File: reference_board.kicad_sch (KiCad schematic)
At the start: 5 parts, among them J1 CONN_02X04, U1 TMP236

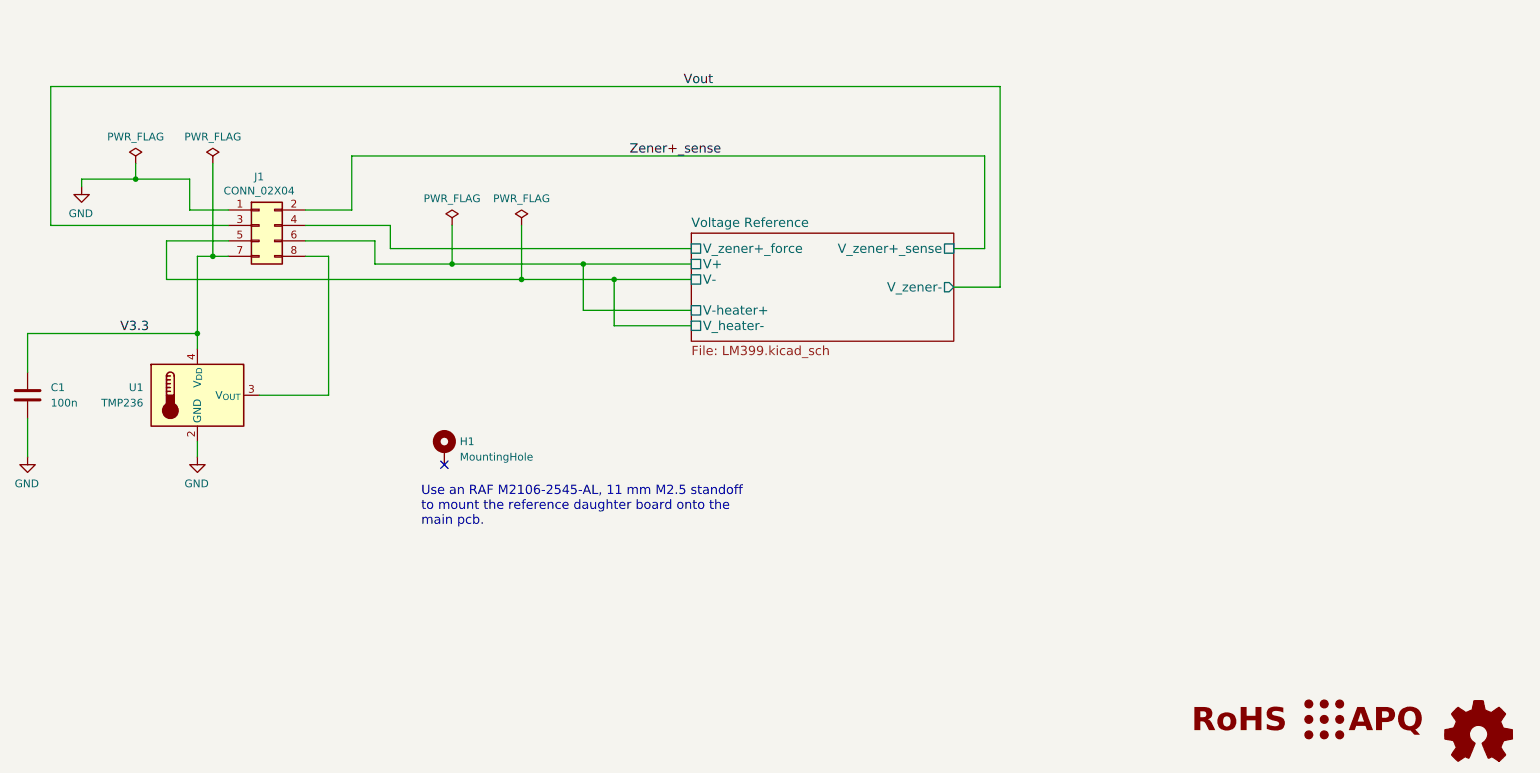
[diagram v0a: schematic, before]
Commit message: Replaced connector J1 with Molex SlimStack 53307-1071.
- Updated to KiCAD 10
- Changed BAS116 diode D1 footprint to SOD-123F due to availability of parts
- Added QED logo
- Removed most references to LM399. The ADR1399 is now the default. LM399 is mentioned as option.
- Added more details for different zener voltage configurations
- Added WEEE logo
- Fixed label on silkscreen refering to R1 instead of R2. It now reads 'R2: 10 ppm/K max.'
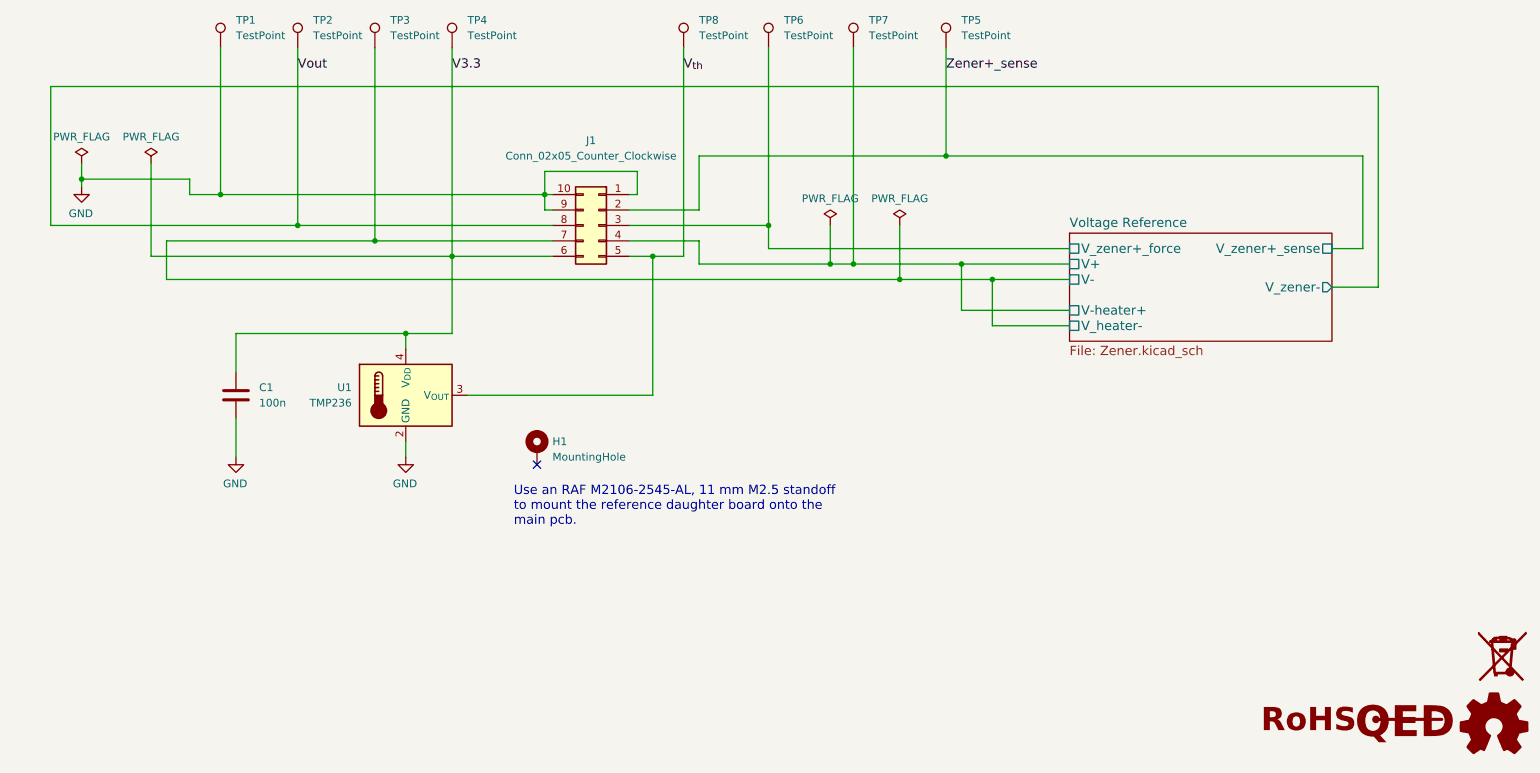
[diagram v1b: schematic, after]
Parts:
- removed J1: CONN_02X04, Connector_PinSocket_2.54mm:PinSocket_2x04_P2.54mm_Vertical, symbol Connector_Generic:Conn_02x04_Odd_Even
- added J1: Conn_02x05_Counter_Clockwise, Custom_footprints_project:Molex_SlimStack_53307-1071_2x05_P0.80mm_Vertical, symbol Connector_Generic:Conn_02x05_Counter_Clockwise
- added SYM2: SYM_WEEE, Symbol:WEEE-Logo_4.2x6mm_SilkScreen, symbol Custom_logos:SYM_WEEE
- added TP1, TP2, TP3, TP4, TP5, TP6, TP7, TP8: TestPoint, TestPoint:TestPoint_Pad_D1.5mm, symbol Connector:TestPoint
- C1: farnell# (none) -> 2070398
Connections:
- net GND: now also J1.1 (Pin_1), J1.10 (Pin_10), J1.9 (Pin_9), TP1.1
- net V3.3: now also J1.6 (Pin_6), TP4.1
- net Voltage Reference/V+: now also J1.4 (Pin_4), TP7.1
- net Voltage Reference/V-: now also J1.7 (Pin_7), TP3.1
- net Voltage Reference/V_zener+_force: now also J1.3 (Pin_3), TP6.1
- net Vout: now also J1.8 (Pin_8), TP2.1
- net Zener+_sense: now also J1.2 (Pin_2), TP5.1
- net V_{th}: now reaches U1.3 (V_{OUT})
- net V_{th}: now also J1.5 (Pin_5), TP8.1
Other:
- sheet Voltage Reference: file LM399.kicad_sch -> Zener.kicad_sch
- company: (none) -> Quantum Electronic Devices GmbH
- title: LM399/ADR1399 negative voltage reference -> ADR1399 negative voltage reference
- moved on the sheet: C1, H1, U1

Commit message: Change standoff to WE 9774045151R.
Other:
- note added: "Use a Würth Elektronik 9774045151R, 4.5 mm M2.5 standoff to mount the reference daughter board onto the main pcb."
- note removed: "Use an RAF M2106-2545-AL, 11 mm M2.5 standoff to mount the reference daughter board onto the main pcb."
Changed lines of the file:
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@@
 		(comment 4 "All capacitors are X7R/X8L ceramic unless specified.")
 	)
-	(text "Use an RAF M2106-2545-AL, 11 mm M2.5 standoff\nto mount the reference daughter board onto the\nmain pcb."
+	(text "Use a Würth Elektronik 9774045151R, 4.5 mm M2.5 standoff\nto mount the reference daughter board onto the\nmain pcb."
 		(exclude_from_sim no)
 		(at 116.84 139.7 0)

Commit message: Fixed DRC errors
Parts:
- added LOGO2: Logo_QED, Custom_footprints_project:QED-logo_small, symbol Custom_logos:Logo_QED
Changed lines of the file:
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@@
 		(dnp no)
 		(fields_autoplaced yes)
-		(property "Reference" "#LOGO1"
+		(property "Reference" "LOGO2"
 			(at 269.24 164.465 0)
 			(hide yes)
@@
 			)
 		)
-		(property "Value" "Logo_APQ"
+		(property "Value" "Logo_QED"
 			(at 269.24 177.8 0)
 			(hide yes)
@@
 			)
 		)
-		(property "Footprint" "custom_footprints_project:QED-logo_small"
+		(property "Footprint" "Custom_footprints_project:QED-logo_small"
 			(at 256.54 171.45 0)
 			(hide yes)
@@
 			(project "reference_board"
 				(path "/afb8e687-4a13-41a1-b8c0-89a749e897fe"
-					(reference "#LOGO1")
+					(reference "LOGO2")
 					(unit 1)
 				)
@@
 		(exclude_from_sim yes)
 		(in_bom no)
-		(on_board no)
+		(on_board yes)
 		(in_pos_files yes)
 		(dnp no)
